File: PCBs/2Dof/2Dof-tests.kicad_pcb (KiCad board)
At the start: 2 copper layers, 53.3 x 46 mm, 49 parts, among them J1 Conn_02x07_Odd_Even, J12 RS485, J14 HBA, J17 Servo1, J2 Conn_02x08_Odd_Even, J3 Conn_02x08_Odd_Even, J5 24Vin, J9 Laser Diode, Q1 QServoA, Q6 LaserDiodeT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

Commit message: small fixes + comments
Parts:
- added RServoA2: 330, Resistor_SMD:R_0402_1005Metric_Pad0.72x0.64mm_HandSolder, F.Cu at (161.1, 68.6)
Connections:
- J17 pad 3: /59 -> /50
- J17 pad 4: /62 -> /52
- J3 pad 3: /40 -> /41
- RRS1 pad 2: /39 -> /35
- RRS2 pad 2: /40 -> /41
- RRS3 pad 2: /40 -> /33
- U1 pad 1: /40 -> /33
- U1 pad 2: /40 -> /41
- U1 pad 3: /40 -> /41
- U1 pad 4: /39 -> /35
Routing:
- net +3.3V: track 43.9 -> 23.8 mm
- net /40: track 17.0 -> 12.0 mm
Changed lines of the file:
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@@
 	(net 65 "unconnected-(UHBA1-IN4-Pad12)")
 	(net 66 "unconnected-(UHBA1-IN3-Pad10)")
+	(net 67 "/41")
 	(footprint "Diode_SMD:D_SOD-123"
 		(layer "F.Cu")
@@
 			(layers "F.Cu" "F.Mask" "F.Paste")
 			(roundrect_rratio 0.25)
-			(net 37 "/39")
+			(net 31 "/35")
 			(pintype "passive")
 		)
@@
 			(layers "*.Cu" "*.Mask")
 			(remove_unused_layers no)
-			(net 34 "/40")
+			(net 67 "/41")
 			(pinfunction "Pin_3")
 			(pintype "passive")
@@
 			(layers "F.Cu" "F.Mask" "F.Paste")
 			(roundrect_rratio 0.25)
-			(net 34 "/40")
+			(net 39 "/33")
 			(pintype "passive")
 		)
@@
 			(layers "F.Cu" "F.Mask" "F.Paste")
 			(roundrect_rratio 0.25)
-			(net 34 "/40")
+			(net 39 "/33")
 			(pinfunction "RO")
 			(pintype "output")
@@
 			(layers "F.Cu" "F.Mask" "F.Paste")
 			(roundrect_rratio 0.25)
-			(net 34 "/40")
+			(net 67 "/41")
 			(pinfunction "~{RE}")
 			(pintype "input")
@@
 			(layers "F.Cu" "F.Mask" "F.Paste")
 			(roundrect_rratio 0.25)
-			(net 34 "/40")
+			(net 67 "/41")
 			(pinfunction "DE")
 			(pintype "input")
@@
 			(layers "F.Cu" "F.Mask" "F.Paste")
 			(roundrect_rratio 0.25)
-			(net 37 "/39")
+			(net 31 "/35")
 			(pinfunction "DI")
 			(pintype "input")
@@
 			(layers "F.Cu" "F.Mask" "F.Paste")
 			(roundrect_rratio 0.25)
-			(net 20 "/59")
+			(net 18 "/50")
 			(pinfunction "Pin_3")
 			(pintype "passive")
@@
 			(layers "F.Cu" "F.Mask" "F.Paste")
 			(roundrect_rratio 0.25)
-			(net 16 "/62")
+			(net 23 "/52")
 			(pinfunction "Pin_4")
 			(pintype "passive")
@@
 	(footprint "Resistor_SMD:R_0402_1005Metric_Pad0.72x0.64mm_HandSolder"
 		(layer "F.Cu")
+		(at 161.0525 68.58)
+		(descr "Resistor SMD 0402 (1005 Metric), square (rectangular) end terminal, IPC-7351 nominal with elongated pad for handsoldering. (Body size source: IPC-SM-782 page 72, https://www.pcb-3d.com/wordpress/wp-content/uploads/ipc-sm-782a_amendment_1_and_2.pdf), generated with kicad-footprint-generator")
+		(tags "resistor handsolder")
+		(property "Reference" "RServoA2"
+			(at 0 -1.17 0)
+			(layer "F.SilkS")
+			(effects
+				(font
+					(size 1 1)
+					(thickness 0.15)
+				)
+			)
+		)
+		(property "Value" "330"
+			(at 0 1.17 0)
+			(layer "F.Fab")
+			(effects
+				(font
+					(size 1 1)
+					(thickness 0.15)
+				)
+			)
+		)
+		(property "Datasheet" "~"
+			(at 0 0 0)
+			(layer "F.Fab")
+			(hide yes)
+			(effects
+				(font
+					(size 1.27 1.27)
+					(thickness 0.15)
+				)
+			)
+		)
+		(property "Description" "Resistor"
+			(at 0 0 0)
+			(layer "F.Fab")
+			(hide yes)
+			(effects
+				(font
+					(size 1.27 1.27)
+					(thickness 0.15)
+				)
+			)
+		)
+		(property ki_fp_filters "R_*")
+		(sheetname "/")
+		(sheetfile "2Dof-tests.kicad_sch")
+		(attr smd)
+		(fp_line
+			(start -0.167621 -0.38)
+			(end 0.167621 -0.38)
+			(stroke
+				(width 0.12)
+				(type solid)
+			)
+			(layer "F.SilkS")
+		)
+		(fp_line
+			(start -0.167621 0.38)
+			(end 0.167621 0.38)
+			(stroke
+				(width 0.12)
+				(type solid)
+			)
+			(layer "F.SilkS")
+		)
+		(fp_rect
+			(start -1.11 -0.47)
+			(end 1.11 0.47)
+			(stroke
+				(width 0.05)
+				(type solid)
+			)
+			(fill no)
+			(layer "F.CrtYd")
+		)
+		(fp_rect
+			(start -0.525 -0.27)
+			(end 0.525 0.27)
+			(stroke
+				(width 0.1)
+				(type solid)
+			)
+			(fill no)
+			(layer "F.Fab")
+		)
+		(fp_text user "${REFERENCE}"
+			(at 0 0 0)
+			(layer "F.Fab")
+			(effects
+				(font
+					(size 0.26 0.26)
+					(thickness 0.04)
+				)
+			)
+		)
+		(pad "1" smd roundrect
+			(at -0.5975 0)
+			(size 0.715 0.64)
+			(layers "F.Cu" "F.Mask" "F.Paste")
+			(roundrect_rratio 0.25)
+			(net 61 "Net-(QServoA1-B)")
+			(pintype "passive")
+		)
+		(pad "2" smd roundrect
+			(at 0.5975 0)
+			(size 0.715 0.64)
+			(layers "F.Cu" "F.Mask" "F.Paste")
+			(roundrect_rratio 0.25)
+			(net 19 "+5V")
+			(pintype "passive")
+		)
+		(embedded_fonts no)
+		(model "${KICAD9_3DMODEL_DIR}/Resistor_SMD.3dshapes/R_0402_1005Metric.step"
+			(offset
+				(xyz 0 0 0)
+			)
+			(scale
+				(xyz 1 1 1)
+			)
+			(rotate
+				(xyz 0 0 0)
+			)
+		)
+	)
+	(footprint "Resistor_SMD:R_0402_1005Metric_Pad0.72x0.64mm_HandSolder"
+		(layer "F.Cu")
 		(at 135.382 73.66 90)
 		(descr "Resistor SMD 0402 (1005 Metric), square (rectangular) end terminal, IPC-7351 nominal with elongated pad for handsoldering. (Body size source: IPC-SM-782 page 72, https://www.pcb-3d.com/wordpress/wp-content/uploads/ipc-sm-782a_amendment_1_and_2.pdf), generated with kicad-footprint-generator")
@@
 			(layers "F.Cu" "F.Mask" "F.Paste")
 			(roundrect_rratio 0.25)
-			(net 34 "/40")
+			(net 67 "/41")
 			(pintype "passive")
 		)
@@
 	)
 	(segment
-		(start 132.745 55.469)
-		(end 132.334 55.88)
-		(width 0.3)
-		(layer "F.Cu")
-		(net 28)
-	)
-	(segment
 		(start 134.239 66.105)
 		(end 134.239 67.5265)
@@
 	)
 	(segment
-		(start 150.321 55.469)
-		(end 132.745 55.469)
-		(width 0.3)
-		(layer "F.Cu")
-		(net 28)
-	)
-	(segment
 		(start 132.334 63.2245)
 		(end 131.609 63.2245)
@@
 	)
 	(segment
-		(start 151.66 54.13)
-		(end 150.321 55.469)
-		(width 0.3)
-		(layer "F.Cu")
-		(net 28)
-	)
-	(segment
 		(start 137.003 83.4305)
 		(end 136.1225 82.55)
@@
 	)
 	(segment
-		(start 132.334 68.2365)
-		(end 131.663 68.9075)
-		(width 0.3)
-		(layer "F.Cu")
-		(net 34)
-	)
-	(segment
 		(start 134.711 73.7335)
 		(end 134.711 75.231)
@@
 	)
 	(segment
-		(start 131.663 68.9075)
-		(end 131.663 69.845098)
-		(width 0.3)
-		(layer "F.Cu")
-		(net 34)
-	)
-	(segment
 		(start 136.779 71.055)
 		(end 135.509 71.055)
@@
 		(width 0.3)
 		(layer "F.Cu")
-		(net 34)
-	)
-	(segment
-		(start 132.872902 71.055)
-		(end 134.239 71.055)
-		(width 0.3)
-		(layer "F.Cu")
-		(net 34)
-	)
-	(segment
-		(start 131.663 69.845098)
-		(end 132.872902 71.055)
-		(width 0.3)
-		(layer "F.Cu")

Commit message: RS485 fixes
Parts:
- removed RRS1: 10K, Resistor_SMD:R_0402_1005Metric_Pad0.72x0.64mm_HandSolder
- moved RServoA2 34.8 mm to (130.8, 51.3), turned to 180 degrees
- moved RRS3 18.3 mm to (150.6, 70.1)
- moved RRS5 17.7 mm to (149.9, 71.9), turned to 180 degrees
- moved RRS2 14.4 mm to (149.4, 70.1)
- moved RRS6 13.7 mm to (142.5, 73.4), turned to 90 degrees
- moved RRS4 10.8 mm to (141.0, 73.4), turned to 90 degrees
- moved U1 10.2 mm to (146.1, 71.1), turned to -90 degrees
- moved CLD1 0.57 mm to (147.6, 65.8)
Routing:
- net +3.3V: track 23.8 -> 53.8 mm
- net /41: track 0.00 -> 24.6 mm, vias 0 -> 4
- net Net-(J12-Pin_3): track 37.1 -> 21.5 mm, vias 2 -> 0
- net Net-(J12-Pin_2): track 33.7 -> 18.2 mm, vias 2 -> 0
- net /33: track 0.00 -> 14.2 mm
- net /50: track 0.00 -> 12.0 mm
- net /40: track 12.0 -> 0.00 mm
- net /52: track 0.00 -> 10.8 mm
- net /35: track 0.00 -> 10.4 mm, vias 0 -> 1
- net /39: track 9.72 -> 0.00 mm
- net /59: track 12.8 -> 5.93 mm
- net +5V: track 119.6 -> 125.2 mm
- net Net-(QServoA1-B): track 4.14 -> 9.71 mm, vias 0 -> 1
- net /62: track 4.83 -> 0.00 mm
- net GND: track 47.2 -> 44.5 mm, vias 26 -> 24

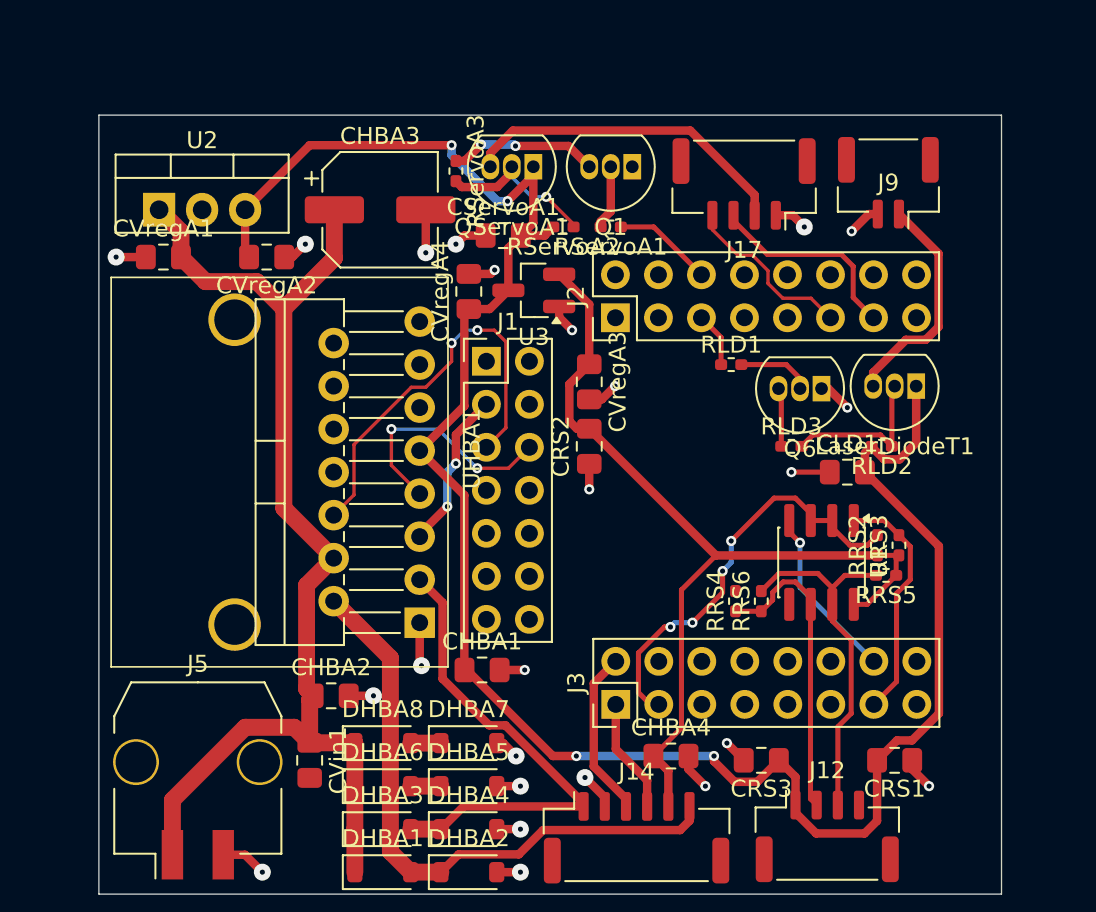
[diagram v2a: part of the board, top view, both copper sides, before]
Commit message: minor silkscreen fixes
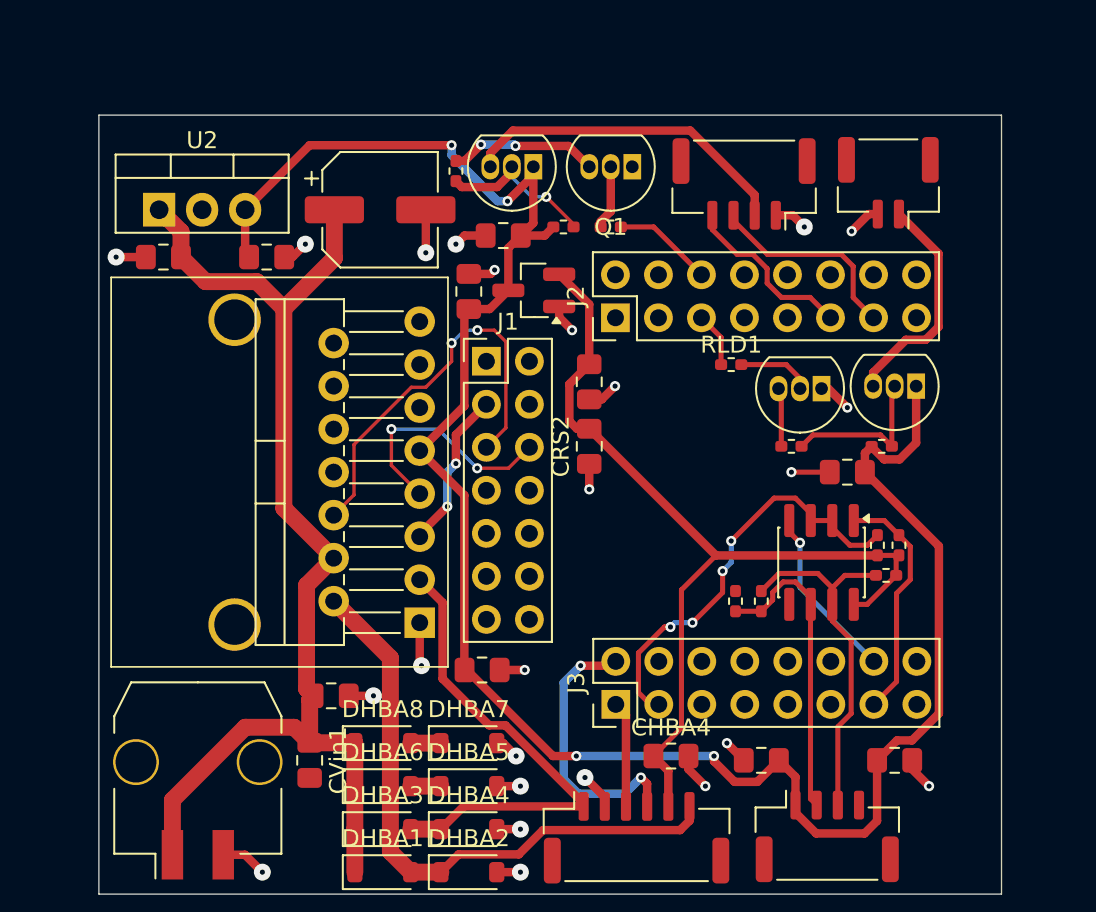
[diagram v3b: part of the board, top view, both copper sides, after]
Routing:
- net /42: track 9.89 -> 16.5 mm, vias 0 -> 2
- net /43: track 6.79 -> 6.28 mm
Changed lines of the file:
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@@
 			(at 0 -1.17 90)
 			(layer "F.SilkS")
+			(hide yes)
 			(effects
 				(font
@@
 			(at 0 -1.68 0)
 			(layer "F.SilkS")
+			(hide yes)
 			(effects
 				(font
@@
 			(at 0 -1.17 90)
 			(layer "F.SilkS")
+			(hide yes)
 			(effects
 				(font
@@
 		(tags "capacitor handsolder")
 		(property "Reference" "CRS1"
-			(at 0 -1.68 0)
+			(at -3.81 0 0)
 			(layer "F.SilkS")
+			(hide yes)
 			(effects
 				(font
@@
 			(at 0 -1.17 0)
 			(layer "F.SilkS")
+			(hide yes)
 			(effects
 				(font
@@
 			(at 0 -4.35 0)
 			(layer "F.SilkS")
+			(hide yes)
 			(effects
 				(font
@@
 			(at 0 -3.9 0)
 			(layer "F.SilkS")
+			(hide yes)
 			(effects
 				(font
@@
 			(at 0 -1.17 0)
 			(layer "F.SilkS")
+			(hide yes)
 			(effects
 				(font
@@
 			(at 0 -1.17 90)
 			(layer "F.SilkS")
+			(hide yes)
 			(effects
 				(font
@@
 			(at 0 -1.68 0)
 			(layer "F.SilkS")
+			(hide yes)
 			(effects
 				(font
@@
 			(at 0 -1.17 0)
 			(layer "F.SilkS")
+			(hide yes)
 			(effects
 				(font
@@
 			(at 0 -1.68 0)
 			(layer "F.SilkS")
+			(hide yes)
 			(effects
 				(font
@@
 			(at 0 -1.68 0)
 			(layer "F.SilkS")
+			(hide yes)
 			(effects
 				(font
@@
 			(at 0 -3.4 90)
 			(layer "F.SilkS")
+			(hide yes)
 			(effects
 				(font
@@
 			(at 0 -6.15 0)
 			(layer "F.SilkS")
+			(hide yes)
 			(effects
 				(font
@@
 			(at 0 -1.68 90)
 			(layer "F.SilkS")
+			(hide yes)
 			(effects
 				(font
@@
 		(tags "to-92 sc-43 sc-43a sot54 PA33 transistor")
 		(property "Reference" "LaserDiodeT1"
-			(at 1.27 -3.56 0)
+			(at -5.842 -4.318 0)
 			(layer "F.SilkS")
+			(hide yes)
 			(effects
 				(font
@@
 			(unlocked yes)
 			(layer "F.SilkS")
+			(hide yes)
 			(effects
 				(font
@@
 			(at 0 -1.68 90)
 			(layer "F.SilkS")
+			(hide yes)
 			(effects
 				(font
@@
 			(at 1.27 -3.56 0)
 			(layer "F.SilkS")
+			(hide yes)
 			(effects
 				(font
@@
 			(at 0 -1.17 0)
 			(layer "F.SilkS")
+			(hide yes)
 			(effects
 				(font
@@
 			(at 0 -3.9 0)
 			(layer "F.SilkS")
+			(hide yes)
 			(effects
 				(font
@@
 			(at 0 0 0)
 			(layer "F.SilkS")
+			(hide yes)
 			(effects
 				(font
@@
 			(at 0 -1.17 0)
 			(layer "F.SilkS")
+			(hide yes)
 			(effects
 				(font
@@
 			(at 0 -1.17 90)
 			(layer "F.SilkS")
+			(hide yes)
 			(effects
 				(font
@@
 			(at 0 -1.68 0)
 			(layer "F.SilkS")
+			(hide yes)
 			(effects
 				(font
@@
 			(at 0 -1.68 0)
 			(layer "F.SilkS")
+			(hide yes)
 			(effects
 				(font
@@
 			(at 0 -3.9 0)
 			(layer "F.SilkS")
+			(hide yes)
 			(effects
 				(font
@@
 			(at 1.27 -3.56 0)
 			(layer "F.SilkS")
+			(hide yes)
 			(effects
 				(font
@@
 			(at 0 -1.68 0)
 			(layer "F.SilkS")
+			(hide yes)
 			(effects
 				(font
@@
 			(at 0 -1.17 90)
 			(layer "F.SilkS")
+			(hide yes)
 			(effects
 				(font
@@
 			(at 0 -2.75 0)
 			(layer "F.SilkS")
+			(hide yes)
 			(effects
 				(font
@@
 	)
 	(segment
-		(start 141.111108 52.979)
-		(end 141.97676 52.979)
-		(width 0.2)
-		(layer "F.Cu")
-		(net 23)
-	)
-	(segment
-		(start 139.603 50.618)
-		(end 139.603 50.947)
-		(width 0.5)
+		(start 143.680529 55.469)
+		(end 145.379 55.469)
+		(width 0.3)
 		(layer "F.Cu")
 		(net 23)
 	)
 	(segment
-		(start 143.764 55.519)
-		(end 145.429 55.519)
-		(width 0.2)
+		(start 145.379 55.469)
+		(end 146.58 56.67)
+		(width 0.3)
 		(layer "F.Cu")
 		(net 23)
 	)
 	(segment
-		(start 142.889 53.89124)
-		(end 142.889 54.644)
-		(width 0.2)
+		(start 139.603 50.618)
+		(end 139.603 51.467999)
+		(width 0.3)
 		(layer "F.Cu")
 		(net 23)
 	)
 	(segment
-		(start 139.603 50.618)
-		(end 139.603 51.470892)
-		(width 0.2)
+		(start 141.997471 52.929)
+		(end 142.839 53.770529)
+		(width 0.3)
 		(layer "F.Cu")
 		(net 23)
 	)
 	(segment
-		(start 142.889 54.644)
-		(end 143.764 55.519)
-		(width 0.2)
+		(start 141.064001 52.929)
+		(end 141.997471 52.929)
+		(width 0.3)
 		(layer "F.Cu")
 		(net 23)
 	)
 	(segment
-		(start 139.603 51.470892)
-		(end 141.111108 52.979)
-		(width 0.2)
+		(start 142.839 53.770529)
+		(end 142.839 54.627471)
+		(width 0.3)
 		(layer "F.Cu")
 		(net 23)
 	)
 	(segment
-		(start 141.97676 52.979)
-		(end 142.889 53.89124)
-		(width 0.2)
+		(start 142.839 54.627471)
+		(end 143.680529 55.469)
+		(width 0.3)
 		(layer "F.Cu")
 		(net 23)
 	)
 	(segment
-		(start 145.429 55.519)
-		(end 146.58 56.67)
-		(width 0.2)
+		(start 139.603 51.467999)
+		(end 141.064001 52.929)
+		(width 0.3)
 		(layer "F.Cu")
 		(net 23)
@@
 	)
 	(segment
-		(start 133.9 82.138292)
-		(end 133.9 79.5)
+		(start 134.503 85.526)
+		(end 134.503 80.103)
 		(width 0.5)
 		(layer "F.Cu")
@@
 	)
 	(segment
-		(start 135.753 83.991292)
-		(end 133.9 82.138292)
+		(start 134.503 80.103)
+		(end 133.9 79.5)
 		(width 0.5)
 		(layer "F.Cu")
@@
 	(segment
 		(start 135.753 85.526)
-		(end 135.753 83.991292)
+		(end 135.753 84.191)
 		(width 0.5)
 		(layer "F.Cu")
-		(net 40)
+		(net 46)
 	)
 	(segment
-		(start 134.503 85.0719)
-		(end 134.503 85.526)
+		(start 133.644 77.216)
+		(end 133.9 76.96)
 		(width 0.5)
 		(layer "F.Cu")
@@
 	)
 	(segment
-		(start 132.599 83.1679)
-		(end 134.503 85.0719)
+		(start 131.826 77.216)
+		(end 133.644 77.216)
 		(width 0.5)
 		(layer "F.Cu")
@@
 	)
 	(segment
-		(start 133.9 76.96)
-		(end 132.599 78.261)
+		(start 135.753 84.191)
+		(end 135.382 83.82)
 		(width 0.5)
 		(layer "F.Cu")
 		(net 46)
 	)
+	(via
+		(at 135.382 83.82)
+		(size 0.6)
+		(drill 0.3)
+		(layers "F.Cu" "B.Cu")
+		(net 46)
+	)
+	(via
+		(at 131.826 77.216)
+		(size 0.6)
+		(drill 0.3)
+		(layers "F.Cu" "B.Cu")
+		(net 46)
+	)
 	(segment
-		(start 132.599 78.261)
-		(end 132.599 83.1679)
+		(start 130.821 83.905918)
+		(end 130.821 78.221)
 		(width 0.5)
-		(layer "F.Cu")
+		(layer "B.Cu")
+		(net 46)
+	)
+	(segment
+		(start 131.686082 84.771)
+		(end 130.821 83.905918)
+		(width 0.5)
+		(layer "B.Cu")
+		(net 46)
+	)
+	(segment
+		(start 134.431 84.771)
+		(end 131.686082 84.771)
+		(width 0.5)
+		(layer "B.Cu")
+		(net 46)
+	)
+	(segment
+		(start 130.821 78.221)
+		(end 131.826 77.216)
+		(width 0.5)
+		(layer "B.Cu")
+		(net 46)
+	)
+	(segment
+		(start 135.382 83.82)
+		(end 134.431 84.771)
+		(width 0.5)
+		(layer "B.Cu")
 		(net 46)
 	)

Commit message: diode fixes
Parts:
- removed DHBA5, DHBA6, DHBA7, DHBA8: 1N4148WT, Diode_SMD:D_SOD-123
- moved RServoA3 1.55 mm to (124.2, 46.5)
- moved CHBA1 0.74 mm to (126.7, 77.5)
- moved CVin 0.74 mm to (115.8, 82.1)
- renumbered CVin1 to CVin
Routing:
- net GND: track 44.5 -> 40.7 mm, vias 24 -> 21
- net Net-(DHBA7-K): track 1.78 -> 0.00 mm
- net Net-(DHBA5-K): track 1.78 -> 0.00 mm
- net +24V: track 69.6 -> 68.6 mm
- net Net-(QServoA1-B): track 9.71 -> 10.7 mm
- net +5V: track 125.2 -> 124.4 mm, vias 4 -> 2
- net Net-(DHBA3-A): track 28.7 -> 29.5 mm

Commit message: comments
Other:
- board text added: "not a huge fan of how this trace narrows"
- board text added: "remember to run DRC, you are missing a groudn VIA"
- board text added: "the molex we are using is through hole, and this is backwards anyway"
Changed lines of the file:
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@@
+	)
+	(gr_rect
+		(start 117.02 83.37)
+		(end 142.06 96.82)
+		(stroke
+			(width 0.2)
+			(type default)
+		)
+		(fill no)
+		(layer "F.Cu")
 	)
 	(gr_rect
@@
 		(layer "Edge.Cuts")
 	)
+	(gr_text "remember to run DRC, you are missing a groudn VIA"
+		(at 141 71.96 0)
+		(layer "F.Cu")
+		(effects
+			(font
+				(size 1.5 1.5)
+				(thickness 0.3)
+				(bold yes)
+			)
+			(justify left bottom)
+		)
+	)
+	(gr_text "not a huge fan of how this trace narrows"
+		(at 118.17 94.23 0)
+		(layer "F.Cu")
+		(effects
+			(font
+				(size 1.5 1.5)
+				(thickness 0.3)
+				(bold yes)
+			)
+			(justify left bottom)
+		)
+	)
 	(gr_text "RUN DRC, you are missing some ground VIAS\n\nVias go through layers, throughhole components already go thgrough the layers\nIf you look at the shaded blue part, you'll see theres no {dblquote}bubble{dblquote} around\ntht components that need ground, there is a t shape through them, so they are\nalready connected to ground. Only surface mount pads need them since they\nneed some way to get the ground connection\n\nthe traces going to the motor should be much much thicker, the traces\nThe traces going to the servos and any high current carrying routes\nshould be thicker as well. Similalry if you have a wider trace, you need \na wider via, the via hole should = trace width, and the via diamter should be double\nalso if you have a capacitor with a thick power trace, the ground trace\nshould be equally as thick\n\nConstraints are in the board setup tab... also google... :(\n\nclean up silkscreen by removing the stuff u dont need and putting\nhelpful labels that will make it easy to assemble and use\n\nAlso changr the jst to the standard one we are using\n\nalso avoid 90 degree traces, also the 5V trace in the big square\ni highlighted is super wonky, i dont think it needs to be like that\n\nPlease go through and clean up some traces, you have vias where you \ndont need them like in the smaller square I made, just comb through \nall of em and make sure theres no unnecessary vias, or if there is a \nbetter way to route that specific area\n\nAre u sure U2 has the right footprint, usually vregs are smd?"
 		(at -113.792 151.892 0)
 		(layer "F.Cu")
 		(effects
+			(font
+				(size 1.5 1.5)
+				(thickness 0.3)
+				(bold yes)
+			)
+			(justify left bottom)
+		)
+	)
+	(gr_text "the molex we are using is through hole, and this is backwards anyway\n"
+		(at 100.61 90.31 90)
+		(layer "F.Cu")
+		(effects
